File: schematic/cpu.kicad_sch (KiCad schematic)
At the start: 2 parts, among them U1 Z80CPU

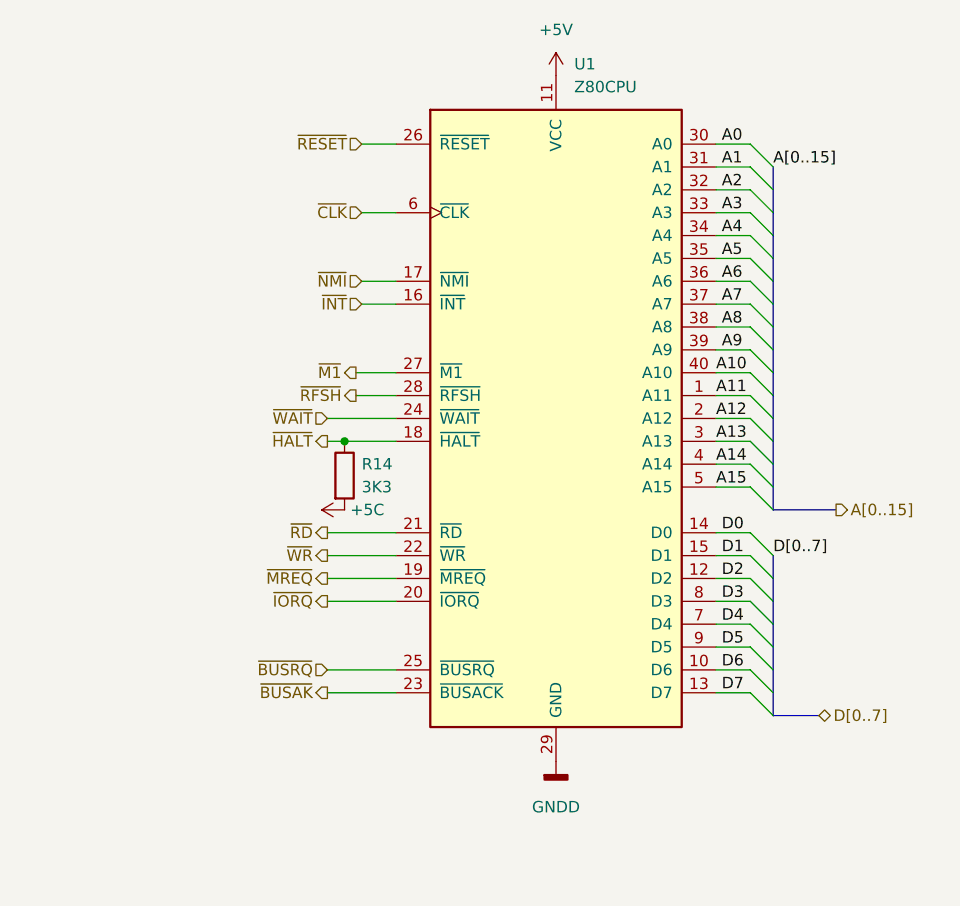
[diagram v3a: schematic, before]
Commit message: fixed some more line names, added a expansion port io pin.
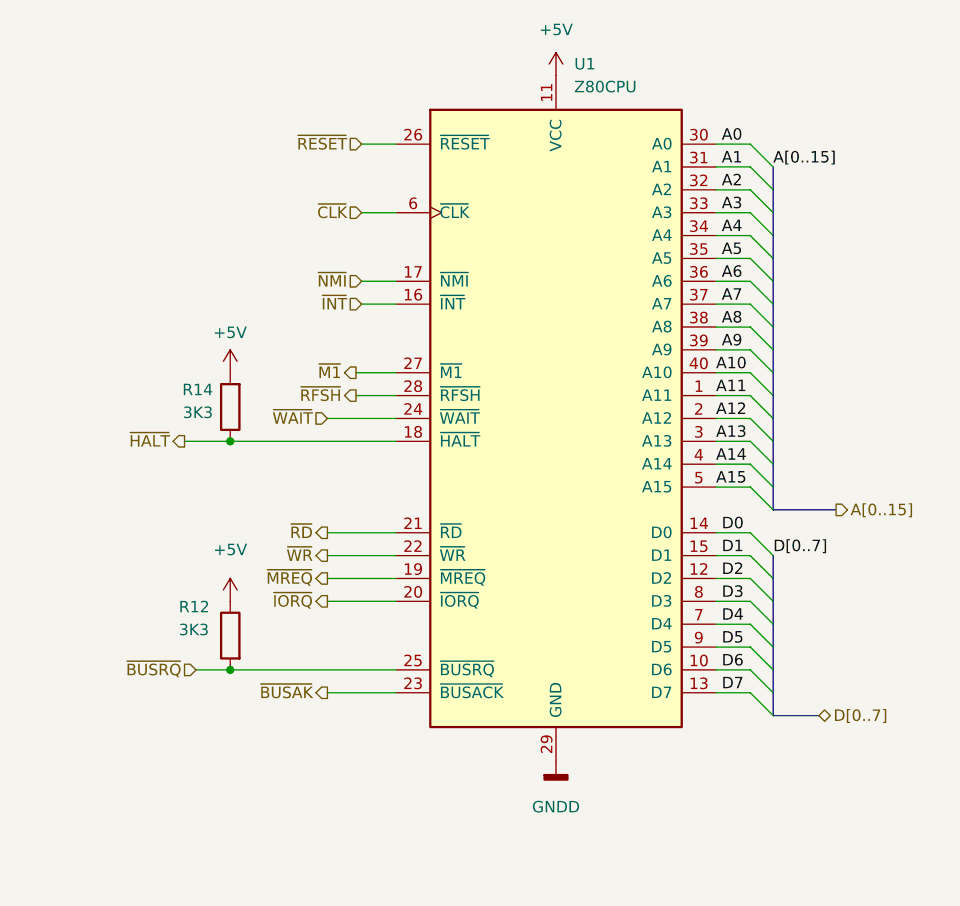
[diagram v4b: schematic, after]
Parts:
- added R12: 3K3, symbol Device:R
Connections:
- net +5C is gone; now on net +5V: R14.2
- net +5V: now also R12.1
- net ~{BUSRQ}: now also R12.2
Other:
- moved on the sheet: R14
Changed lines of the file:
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@@
 (kicad_sch (version 20211123) (generator eeschema)
   (paper "A4")
-  (junction (at 121.92 88.9) (diameter 0) (color 0 0 0 0)
+  (junction (at 109.22 114.3) (diameter 0) (color 0 0 0 0)
+  )
+  (junction (at 109.22 88.9) (diameter 0) (color 0 0 0 0)
   )
   (bus_entry (at 167.005 78.74) (size 2.54 2.54)
@@
     (stroke (width 0) (type default) (color 0 0 0 0))
   )
+  (wire (pts (xy 109.22 88.9) (xy 127.635 88.9))
+    (stroke (width 0) (type default) (color 0 0 0 0))
+  )
   (wire (pts (xy 163.195 106.68) (xy 167.005 106.68))
     (stroke (width 0) (type default) (color 0 0 0 0))
@@
     (stroke (width 0) (type default) (color 0 0 0 0))
   )
-  (wire (pts (xy 121.92 88.9) (xy 127.635 88.9))
+  (wire (pts (xy 104.14 88.9) (xy 109.22 88.9))
     (stroke (width 0) (type default) (color 0 0 0 0))
   )
@@
     (stroke (width 0) (type default) (color 0 0 0 0))
   )
-  (wire (pts (xy 120.015 114.3) (xy 127.635 114.3))
+  (wire (pts (xy 105.41 114.3) (xy 109.22 114.3))
     (stroke (width 0) (type default) (color 0 0 0 0))
   )
@@
     (stroke (width 0) (type default) (color 0 0 0 0))
   )
+  (wire (pts (xy 109.22 114.3) (xy 127.635 114.3))
+    (stroke (width 0) (type default) (color 0 0 0 0))
+  )
   (wire (pts (xy 163.195 55.88) (xy 167.005 55.88))
     (stroke (width 0) (type default) (color 0 0 0 0))
   )
-  (wire (pts (xy 120.015 88.9) (xy 121.92 88.9))
-    (stroke (width 0) (type default) (color 0 0 0 0))
-  )
   (wire (pts (xy 163.195 73.66) (xy 167.005 73.66))
     (stroke (width 0) (type default) (color 0 0 0 0))
@@
     (effects (font (size 1.27 1.27)) (justify left bottom))
   )
-  (hierarchical_label "~{BUSRQ}" (shape input) (at 120.015 114.3 180)
+  (hierarchical_label "~{BUSRQ}" (shape input) (at 105.41 114.3 180)
     (effects (font (size 1.27 1.27)) (justify right))
   )
@@
     (effects (font (size 1.27 1.27)) (justify left))
   )
-  (hierarchical_label "~{HALT}" (shape output) (at 120.015 88.9 180)
+  (hierarchical_label "~{HALT}" (shape output) (at 104.14 88.9 180)
     (effects (font (size 1.27 1.27)) (justify right))
   )
@@
     )
     (pin "1")
+  )
+  (symbol (lib_id "Device:R") (at 109.22 110.49 0) (mirror y) (unit 1)
+    (in_bom yes) (on_board yes)
+    (property "Reference" "R12" (id 0) (at 103.505 107.315 0)
+      (effects (font (size 1.27 1.27)) (justify right))
+    )
+    (property "Value" "3K3" (id 1) (at 103.505 109.855 0)
+      (effects (font (size 1.27 1.27)) (justify right))
+    )
+    (property "Footprint" "" (id 2) (at 110.998 110.49 90)
+      (effects (font (size 1.27 1.27)) hide)
+    )
+    (property "Datasheet" "~" (id 3) (at 109.22 110.49 0)
+      (effects (font (size 1.27 1.27)) hide)
+    )
+    (pin "1")
+    (pin "2")
   )
   (symbol (lib_id "CPU:Z80CPU") (at 145.415 86.36 0) (unit 1)
@@
     (pin "9")
   )
-  (symbol (lib_id "power:+5C") (at 121.92 96.52 90) (unit 1)
-    (in_bom yes) (on_board yes) (fields_autoplaced)
-    (property "Reference" "#PWR?" (id 0) (at 125.73 96.52 0)
-      (effects (font (size 1.27 1.27)) hide)
-    )
-    (property "Value" "+5C" (id 1) (at 122.555 96.5199 90)
-      (effects (font (size 1.27 1.27)) (justify right))
-    )
-    (property "Footprint" "" (id 2) (at 121.92 96.52 0)
-      (effects (font (size 1.27 1.27)) hide)
-    )
-    (property "Datasheet" "" (id 3) (at 121.92 96.52 0)
-      (effects (font (size 1.27 1.27)) hide)
-    )
-    (pin "1")
-  )
   (symbol (lib_id "power:GNDD") (at 145.415 124.46 0) (unit 1)
     (in_bom yes) (on_board yes) (fields_autoplaced)
@@
     (pin "1")
   )
-  (symbol (lib_id "Device:R") (at 121.92 92.71 0) (unit 1)
+  (symbol (lib_id "Device:R") (at 109.22 85.09 180) (unit 1)
+    (in_bom yes) (on_board yes)
+    (property "Reference" "R14" (id 0) (at 107.315 83.185 0)
+      (effects (font (size 1.27 1.27)) (justify left))
+    )
+    (property "Value" "3K3" (id 1) (at 107.315 85.725 0)
+      (effects (font (size 1.27 1.27)) (justify left))
+    )
+    (property "Footprint" "" (id 2) (at 110.998 85.09 90)
+      (effects (font (size 1.27 1.27)) hide)
+    )
+    (property "Datasheet" "~" (id 3) (at 109.22 85.09 0)
+      (effects (font (size 1.27 1.27)) hide)
+    )
+    (pin "1")
+    (pin "2")
+  )
+  (symbol (lib_id "power:+5V") (at 109.22 106.68 0) (unit 1)
     (in_bom yes) (on_board yes) (fields_autoplaced)
-    (property "Reference" "R14" (id 0) (at 123.825 91.4399 0)
+    (property "Reference" "#PWR?" (id 0) (at 109.22 110.49 0)
+      (effects (font (size 1.27 1.27)) hide)
+    )
+    (property "Value" "+5V" (id 1) (at 109.22 100.965 0))
+    (property "Footprint" "" (id 2) (at 109.22 106.68 0)
+      (effects (font (size 1.27 1.27)) hide)
+    )
+    (property "Datasheet" "" (id 3) (at 109.22 106.68 0)
+      (effects (font (size 1.27 1.27)) hide)
+    )
+    (pin "1")
+  )
+  (symbol (lib_id "power:+5V") (at 109.22 81.28 0) (unit 1)
+    (in_bom yes) (on_board yes)
+    (property "Reference" "#PWR?" (id 0) (at 109.22 85.09 0)
+      (effects (font (size 1.27 1.27)) hide)
+    )
+    (property "Value" "+5V" (id 1) (at 107.315 76.835 0)
       (effects (font (size 1.27 1.27)) (justify left))
     )
-    (property "Value" "3K3" (id 1) (at 123.825 93.9799 0)
-      (effects (font (size 1.27 1.27)) (justify left))
-    )
-    (property "Footprint" "" (id 2) (at 120.142 92.71 90)
-      (effects (font (size 1.27 1.27)) hide)
-    )
-    (property "Datasheet" "~" (id 3) (at 121.92 92.71 0)
-      (effects (font (size 1.27 1.27)) hide)
-    )
-    (pin "1")
-    (pin "2")
+    (property "Footprint" "" (id 2) (at 109.22 81.28 0)
+      (effects (font (size 1.27 1.27)) hide)
+    )
+    (property "Datasheet" "" (id 3) (at 109.22 81.28 0)
+      (effects (font (size 1.27 1.27)) hide)
+    )
+    (pin "1")
   )
 )

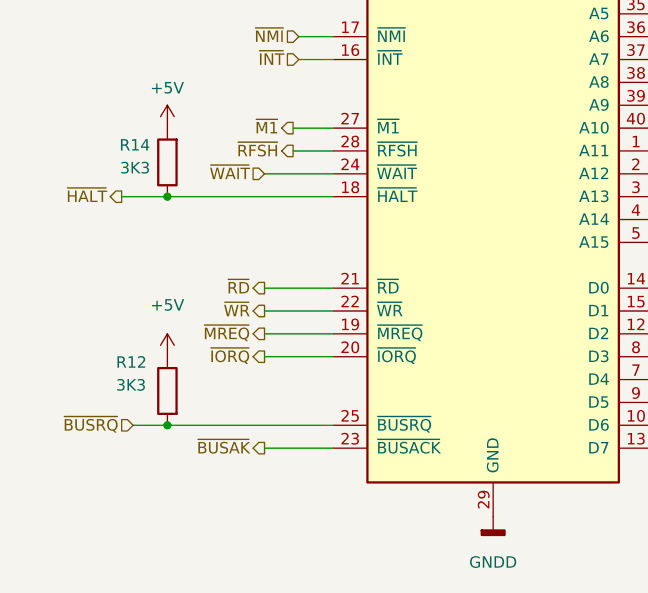
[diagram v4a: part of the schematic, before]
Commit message: Cleanup clock-reset-invert schematic. Checked against wiki.console5.com/wiki/Colecovision. Had a inverter backwards (after cleanup it was obvious since its a standard circuit). Everything else checks, though schematic is missing the wire connection on D8B from 8 to 12. Verified that mine is correct and the wiki is incorrect.
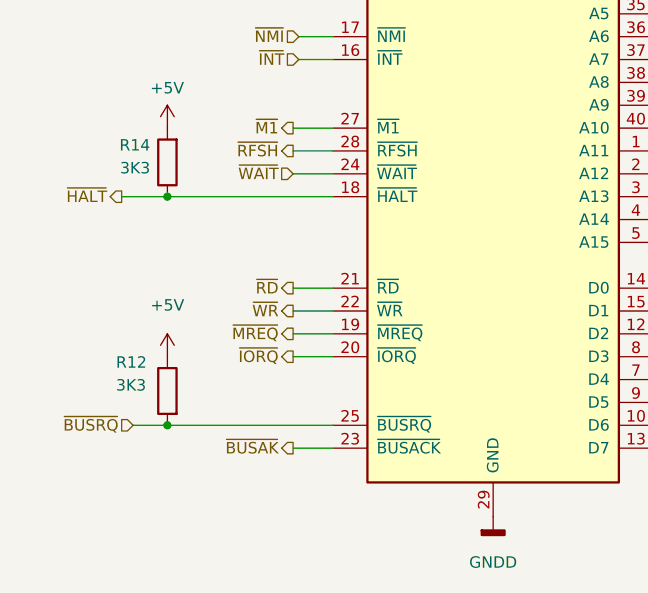
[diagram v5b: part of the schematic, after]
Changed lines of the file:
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@@
     (stroke (width 0) (type default) (color 0 0 0 0))
   )
-  (wire (pts (xy 120.015 104.14) (xy 127.635 104.14))
+  (wire (pts (xy 123.19 104.14) (xy 127.635 104.14))
     (stroke (width 0) (type default) (color 0 0 0 0))
   )
@@
     (stroke (width 0) (type default) (color 0 0 0 0))
   )
-  (wire (pts (xy 120.015 116.84) (xy 127.635 116.84))
+  (wire (pts (xy 123.19 116.84) (xy 127.635 116.84))
     (stroke (width 0) (type default) (color 0 0 0 0))
   )
@@
     (stroke (width 0) (type default) (color 0 0 0 0))
   )
-  (wire (pts (xy 120.015 101.6) (xy 127.635 101.6))
+  (wire (pts (xy 123.19 101.6) (xy 127.635 101.6))
     (stroke (width 0) (type default) (color 0 0 0 0))
   )
@@
     (stroke (width 0) (type default) (color 0 0 0 0))
   )
-  (wire (pts (xy 120.015 99.06) (xy 127.635 99.06))
+  (wire (pts (xy 123.19 99.06) (xy 127.635 99.06))
     (stroke (width 0) (type default) (color 0 0 0 0))
   )
@@
     (stroke (width 0) (type default) (color 0 0 0 0))
   )
-  (wire (pts (xy 120.015 86.36) (xy 127.635 86.36))
+  (wire (pts (xy 123.19 86.36) (xy 127.635 86.36))
     (stroke (width 0) (type default) (color 0 0 0 0))
   )
@@
     (stroke (width 0) (type default) (color 0 0 0 0))
   )
-  (wire (pts (xy 120.015 106.68) (xy 127.635 106.68))
+  (wire (pts (xy 123.19 106.68) (xy 127.635 106.68))
     (stroke (width 0) (type default) (color 0 0 0 0))
   )
@@
     (effects (font (size 1.27 1.27)) (justify right))
   )
-  (hierarchical_label "~{WR}" (shape output) (at 120.015 101.6 180)
-    (effects (font (size 1.27 1.27)) (justify right))
-  )
-  (hierarchical_label "~{RD}" (shape output) (at 120.015 99.06 180)
+  (hierarchical_label "~{WR}" (shape output) (at 123.19 101.6 180)
+    (effects (font (size 1.27 1.27)) (justify right))
+  )
+  (hierarchical_label "~{RD}" (shape output) (at 123.19 99.06 180)
     (effects (font (size 1.27 1.27)) (justify right))
   )
@@
     (effects (font (size 1.27 1.27)) (justify right))
   )
-  (hierarchical_label "~{MREQ}" (shape output) (at 120.015 104.14 180)
-    (effects (font (size 1.27 1.27)) (justify right))
-  )
-  (hierarchical_label "~{BUSAK}" (shape output) (at 120.015 116.84 180)
+  (hierarchical_label "~{MREQ}" (shape output) (at 123.19 104.14 180)
+    (effects (font (size 1.27 1.27)) (justify right))
+  )
+  (hierarchical_label "~{BUSAK}" (shape output) (at 123.19 116.84 180)
     (effects (font (size 1.27 1.27)) (justify right))
   )
@@
     (effects (font (size 1.27 1.27)) (justify right))
   )
-  (hierarchical_label "~{WAIT}" (shape input) (at 120.015 86.36 180)
+  (hierarchical_label "~{WAIT}" (shape input) (at 123.19 86.36 180)
     (effects (font (size 1.27 1.27)) (justify right))
   )
@@
     (effects (font (size 1.27 1.27)) (justify right))
   )
-  (hierarchical_label "~{IORQ}" (shape output) (at 120.015 106.68 180)
-    (effects (font (size 1.27 1.27)) (justify right))
-  )
+  (hierarchical_label "~{IORQ}" (shape output) (at 123.19 106.68 180)
+    (effects (font (size 1.27 1.27)) (justify right))
+  )

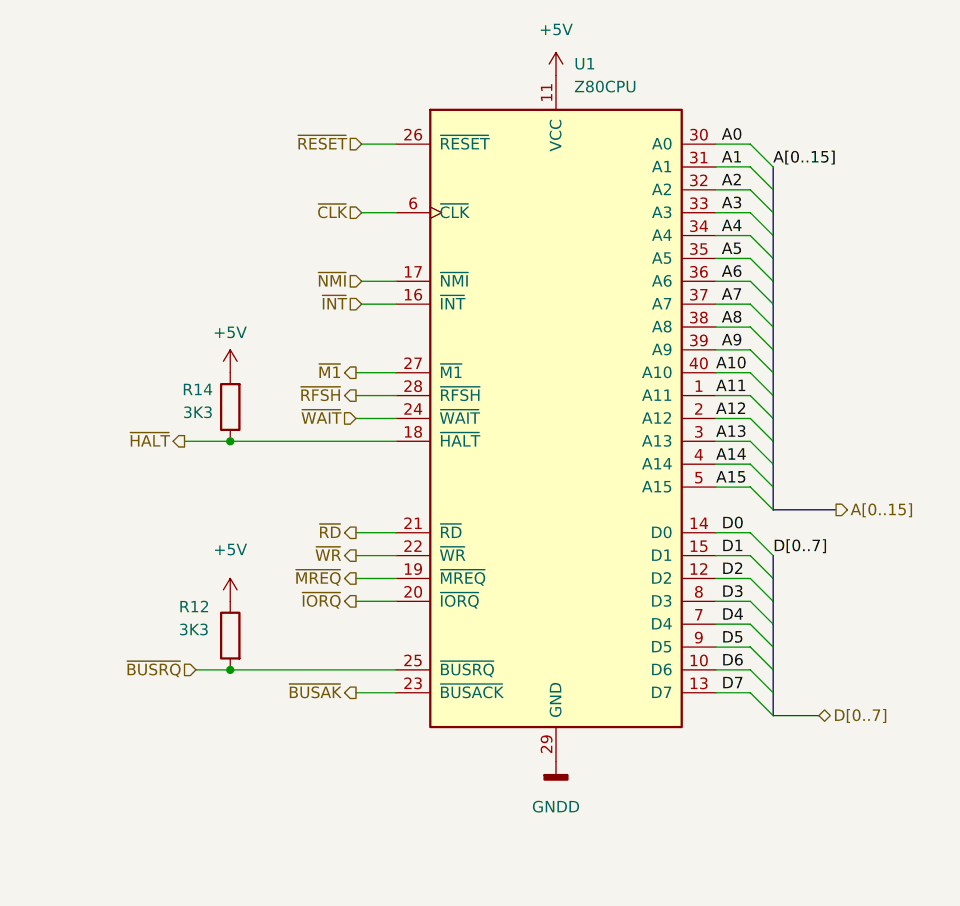
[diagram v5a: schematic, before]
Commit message: adjusted size of the sheets. added pcb version to the rev field. F.0... the 0 is for future fixes on my end. RF PCB is E.0.
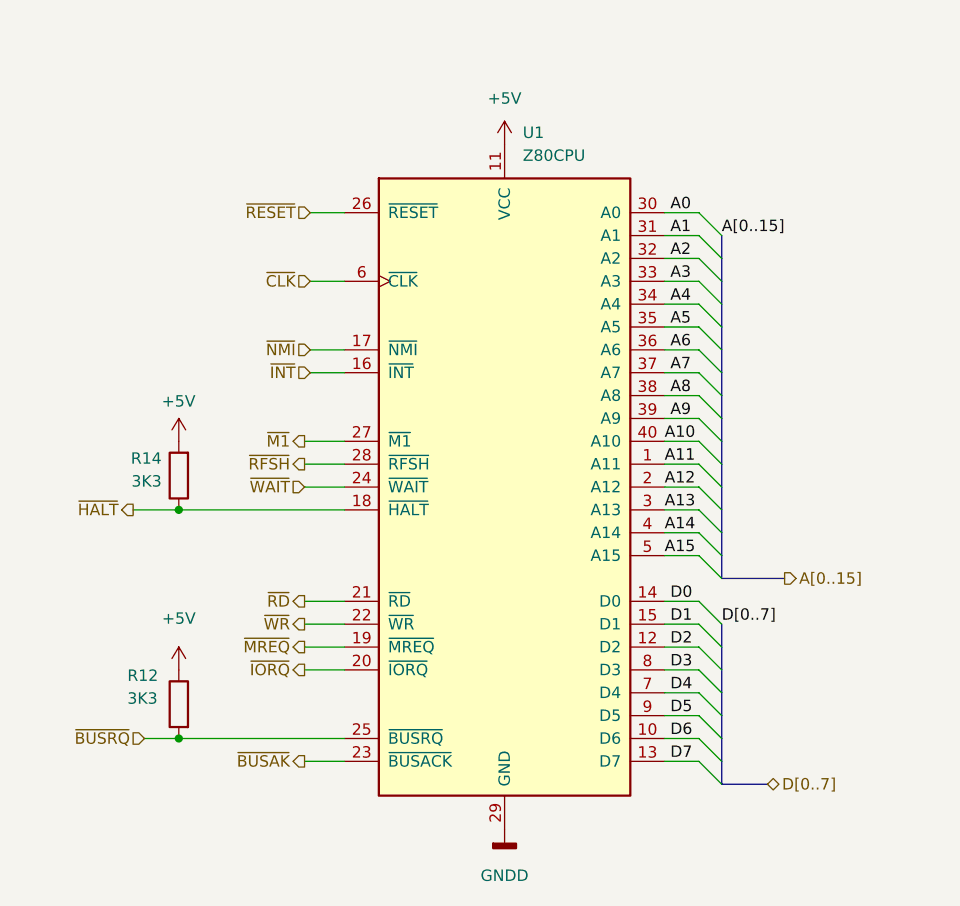
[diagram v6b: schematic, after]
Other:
- title: (none) -> Colecovision Schematic
- moved on the sheet: R12, R14, U1

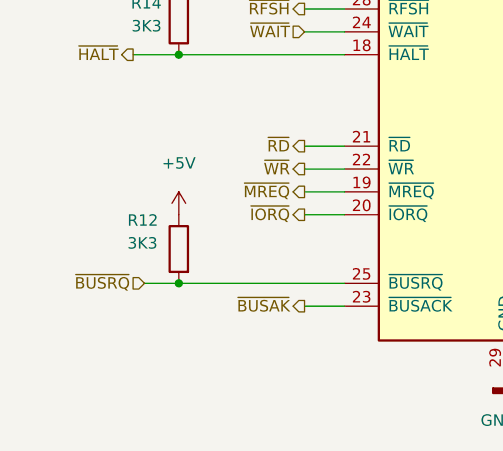
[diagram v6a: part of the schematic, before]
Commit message: cleanup, and started associating components
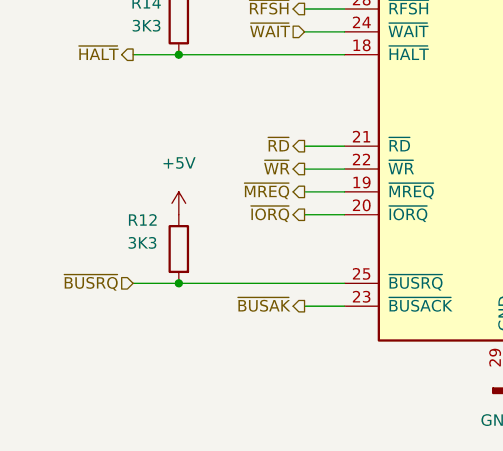
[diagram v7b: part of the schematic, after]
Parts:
- R12, R14: footprint (none) -> Resistor_THT:R_Axial_DIN0207_L6.3mm_D2.5mm_P7.62mm_Horizontal
- U1: footprint (none) -> Package_DIP:DIP-40_W15.24mm_LongPads
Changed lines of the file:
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@@
     (stroke (width 0) (type default) (color 0 0 0 0))
   )
-  (wire (pts (xy 99.695 121.92) (xy 103.505 121.92))
+  (wire (pts (xy 98.425 121.92) (xy 103.505 121.92))
     (stroke (width 0) (type default) (color 0 0 0 0))
   )
@@
     (effects (font (size 1.27 1.27)) (justify left bottom))
   )
-  (hierarchical_label "~{BUSRQ}" (shape input) (at 99.695 121.92 180)
+  (hierarchical_label "~{BUSRQ}" (shape input) (at 98.425 121.92 180)
     (effects (font (size 1.27 1.27)) (justify right))
   )
@@
   (symbol (lib_id "power:+5V") (at 139.7 55.88 0) (unit 1)
     (in_bom yes) (on_board yes) (fields_autoplaced)
-    (property "Reference" "#PWR?" (id 0) (at 139.7 59.69 0)
+    (property "Reference" "#PWR0127" (id 0) (at 139.7 59.69 0)
       (effects (font (size 1.27 1.27)) hide)
     )
@@
       (effects (font (size 1.27 1.27)) (justify right))
     )
-    (property "Footprint" "" (id 2) (at 105.283 118.11 90)
+    (property "Footprint" "Resistor_THT:R_Axial_DIN0207_L6.3mm_D2.5mm_P7.62mm_Horizontal" (id 2) (at 105.283 118.11 90)
       (effects (font (size 1.27 1.27)) hide)
     )
@@
       (effects (font (size 1.27 1.27)) (justify left))
     )
-    (property "Footprint" "" (id 2) (at 139.7 83.82 0)
+    (property "Footprint" "Package_DIP:DIP-40_W15.24mm_LongPads" (id 2) (at 139.7 83.82 0)
       (effects (font (size 1.27 1.27)) hide)
     )
@@
   (symbol (lib_id "power:GNDD") (at 139.7 132.08 0) (unit 1)
     (in_bom yes) (on_board yes) (fields_autoplaced)
-    (property "Reference" "#PWR?" (id 0) (at 139.7 138.43 0)
+    (property "Reference" "#PWR0126" (id 0) (at 139.7 138.43 0)
       (effects (font (size 1.27 1.27)) hide)
     )
@@
       (effects (font (size 1.27 1.27)) (justify left))
     )
-    (property "Footprint" "" (id 2) (at 105.283 92.71 90)
+    (property "Footprint" "Resistor_THT:R_Axial_DIN0207_L6.3mm_D2.5mm_P7.62mm_Horizontal" (id 2) (at 105.283 92.71 90)
       (effects (font (size 1.27 1.27)) hide)
     )
@@
   (symbol (lib_id "power:+5V") (at 103.505 114.3 0) (unit 1)
     (in_bom yes) (on_board yes) (fields_autoplaced)
-    (property "Reference" "#PWR?" (id 0) (at 103.505 118.11 0)
+    (property "Reference" "#PWR0128" (id 0) (at 103.505 118.11 0)
       (effects (font (size 1.27 1.27)) hide)
     )
@@
   (symbol (lib_id "power:+5V") (at 103.505 88.9 0) (unit 1)
     (in_bom yes) (on_board yes)
-    (property "Reference" "#PWR?" (id 0) (at 103.505 92.71 0)
-      (effects (font (size 1.27 1.27)) hide)
-    )
+    (property "Reference" "#PWR0129" (id 0) (at 103.505 92.71 0)
+      (effects (font (size 1.27 1.27)) hide)
+    )
